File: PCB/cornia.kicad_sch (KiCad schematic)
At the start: 78 parts, among them J1 Conn_01x01_Pin, SW1 SW_Push, SW10 SW_Push, SW11 SW_Push, SW12 SW_Push, SW13 SW_Push, SW14 SW_Push, SW15 SW_Push, SW16 SW_Push, SW17 SW_Push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

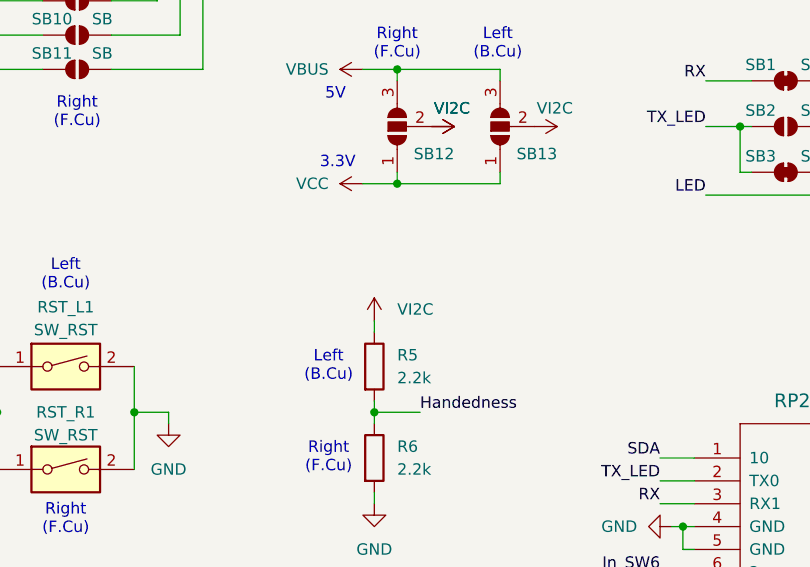
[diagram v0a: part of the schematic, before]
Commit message: [PCB] Fix handedness pin voltage (fixed to 3v3)
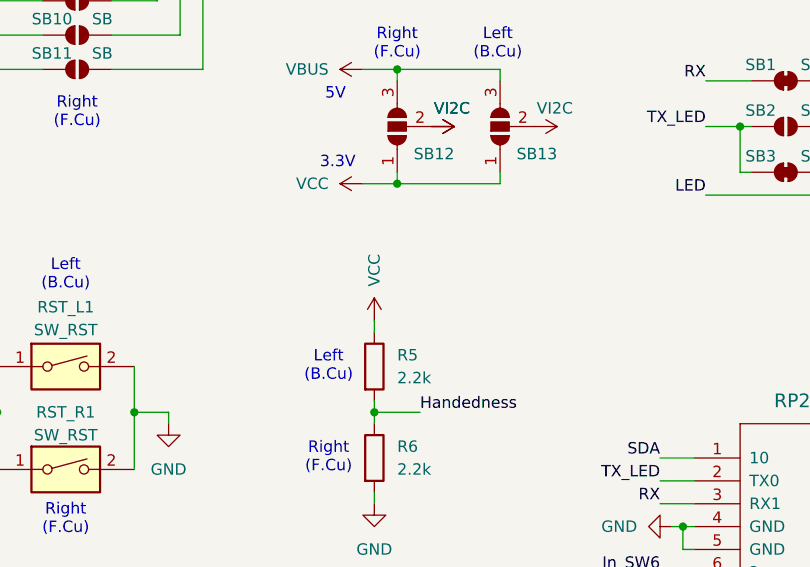
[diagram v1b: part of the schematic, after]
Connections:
- net VCC: now also R5.1
- net VI2C: no longer R5.1
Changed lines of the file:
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@@
-	)
-	(symbol
-		(lib_id "power:VBUS")
-		(at 191.77 90.17 0)
-		(unit 1)
-		(exclude_from_sim no)
-		(in_bom yes)
-		(on_board yes)
-		(dnp no)
-		(fields_autoplaced yes)
-		(property "Reference" "#PWR077"
-			(at 191.77 93.98 0)
-			(effects
-				(font
-					(size 1.27 1.27)
-				)
-				(hide yes)
-			)
-		)
-		(property "Value" "VI2C"
-			(at 194.31 88.8999 0)
-			(effects
-				(font
-					(size 1.27 1.27)
-				)
-				(justify left)
-			)
-		)
-		(property "Footprint" ""
-			(at 191.77 90.17 0)
-			(effects
-				(font
-					(size 1.27 1.27)
-				)
-				(hide yes)
-			)
-		)
-		(property "Datasheet" ""
-			(at 191.77 90.17 0)
-			(effects
-				(font
-					(size 1.27 1.27)
-				)
-				(hide yes)
-			)
-		)
-		(property "Description" "Power symbol creates a global label with name \"VBUS\""
-			(at 191.77 90.17 0)
-			(effects
-				(font
-					(size 1.27 1.27)
-				)
-				(hide yes)
-			)
-		)
-		(pin "1"
-		)
-		(instances
-			(project "cornia"
-				(path "/fba9d1ab-287c-4388-b412-675aea5ffe31"
-					(reference "#PWR077")
-					(unit 1)
-				)
-			)
-		)
 	)
 	(symbol
@@
 					(unit 1)
 				)
+			)
+		)
+	)
+	(symbol
+		(lib_id "power:VBUS")
+		(at 191.77 90.17 0)
+		(unit 1)
+		(exclude_from_sim no)
+		(in_bom yes)
+		(on_board yes)
+		(dnp no)
+		(property "Reference" "#PWR084"
+			(at 191.77 93.98 0)
+			(effects
+				(font
+					(size 1.27 1.27)
+				)
+				(hide yes)
+			)
+		)
+		(property "Value" "VCC"
+			(at 191.7699 86.36 90)
+			(effects
+				(font
+					(size 1.27 1.27)
+				)
+				(justify left)
+			)
+		)
+		(property "Footprint" ""
+			(at 191.77 90.17 0)
+			(effects
+				(font
+					(size 1.27 1.27)
+				)
+				(hide yes)
+			)
+		)
+		(property "Datasheet" ""
+			(at 191.77 90.17 0)
+			(effects
+				(font
+					(size 1.27 1.27)
+				)
+				(hide yes)
+			)
+		)
+		(property "Description" "Power symbol creates a global label with name \"VBUS\""
+			(at 191.77 90.17 0)
+			(effects
+				(font
+					(size 1.27 1.27)
+				)
+				(hide yes)
+			)
+		)
+		(pin "1"
+		)
+		(instances
+			(project "cornia"
+				(path "/fba9d1ab-287c-4388-b412-675aea5ffe31"
+					(reference "#PWR084")
+					(unit 1)
+				)
